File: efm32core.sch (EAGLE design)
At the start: 14 parts

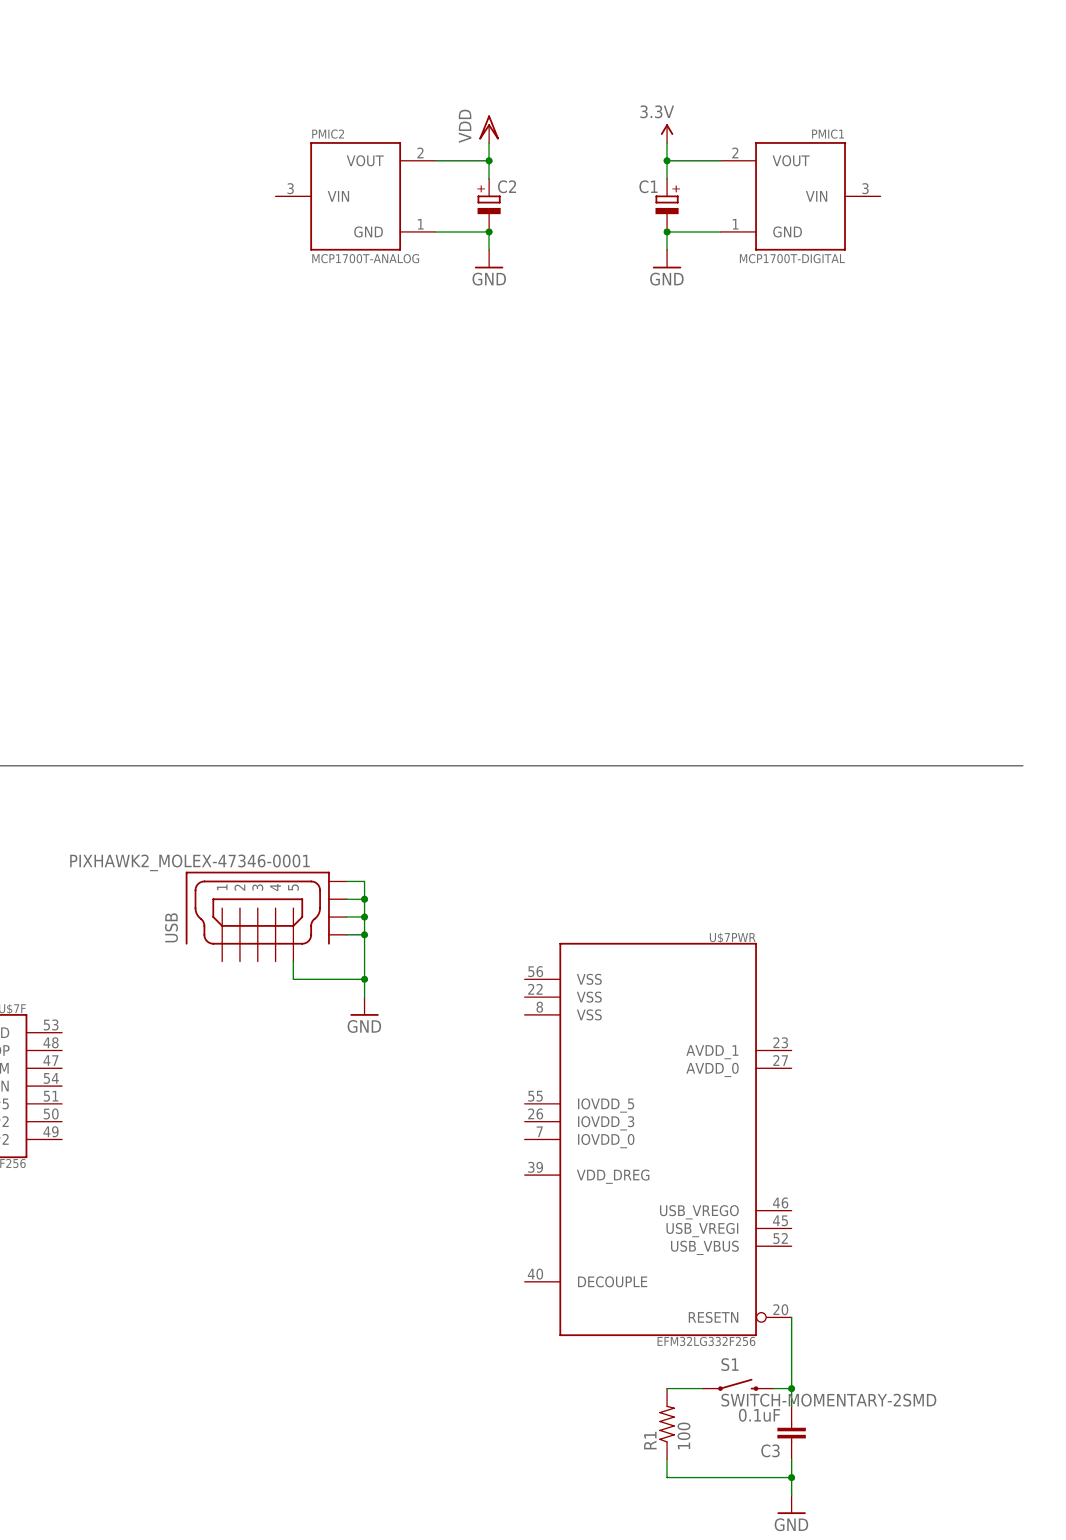
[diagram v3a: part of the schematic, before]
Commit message: optimize board shape
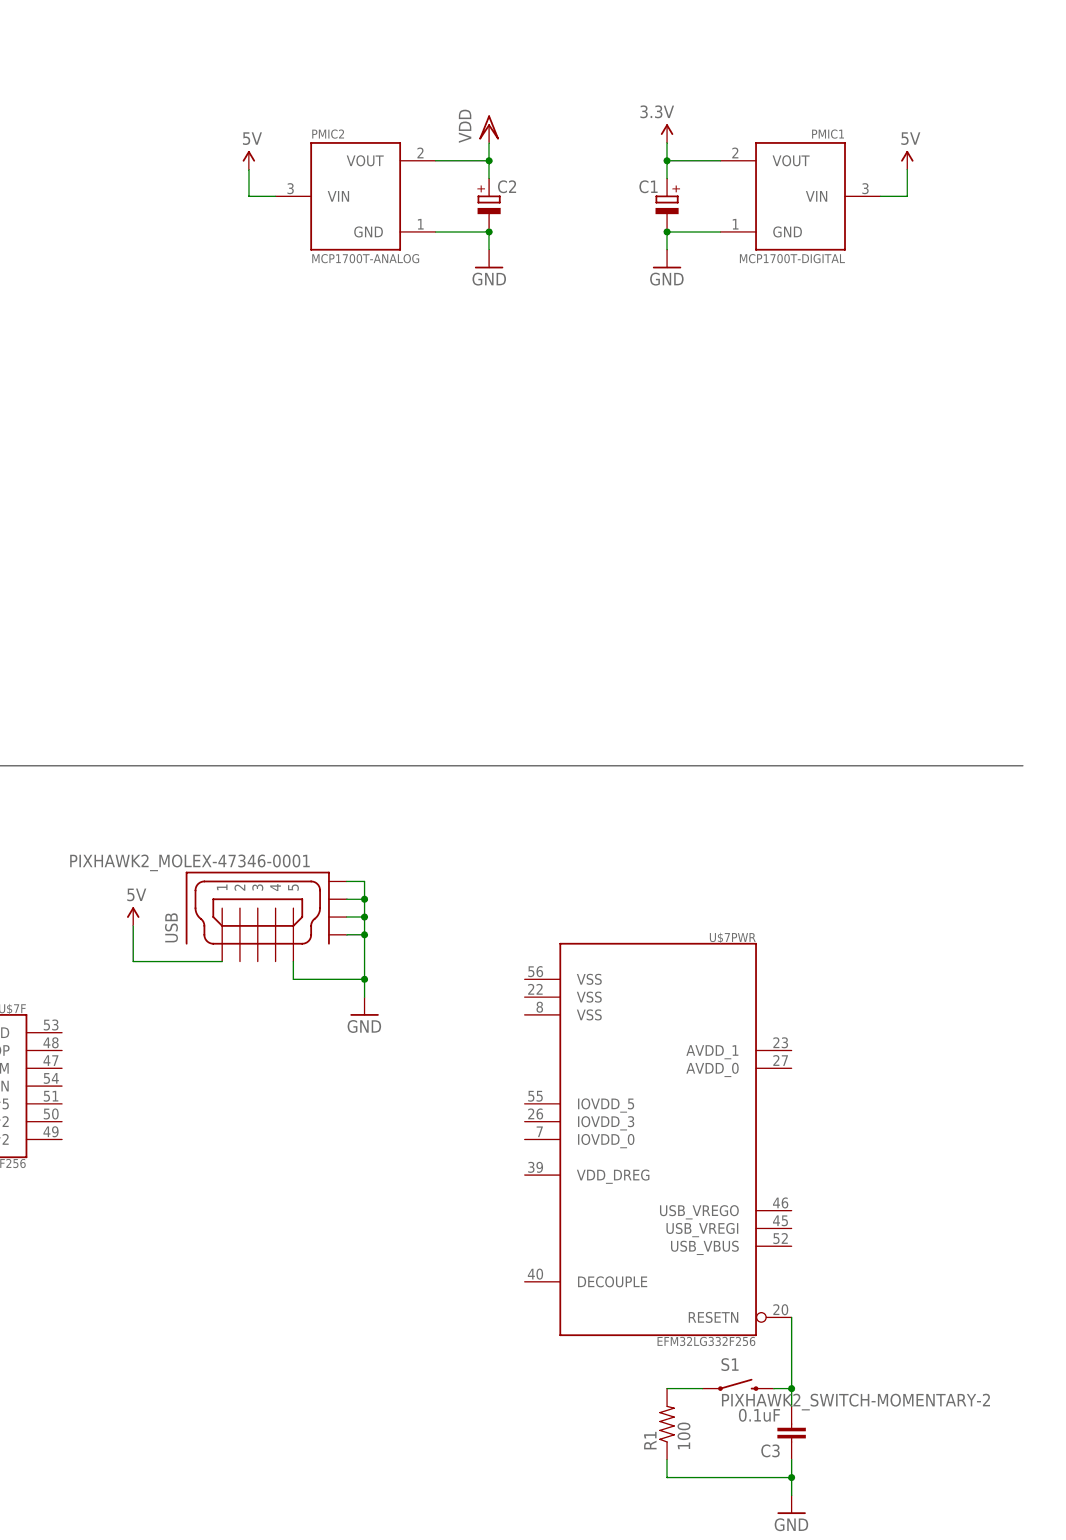
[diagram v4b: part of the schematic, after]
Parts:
- S1: value SWITCH-MOMENTARY-2SMD -> PIXHAWK2_SWITCH-MOMENTARY-2; device SparkFun-Electromechanical:SWITCH-MOMENTARY-2SMD -> PX4FMUv1.7.1:PIXHAWK2_SWITCH-MOMENTARY-2
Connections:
- new net 5V: PMIC1.VIN, PMIC2.VIN, USB.1
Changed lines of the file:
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@@
 <grid distance="0.05" unitdist="inch" unit="inch" style="lines" multiple="1" display="yes" altdistance="0.01" altunitdist="inch" altunit="inch"/>
 <layers>
-<layer number="1" name="Top" color="4" fill="1" visible="no" active="no"/>
-<layer number="16" name="Bottom" color="1" fill="1" visible="no" active="no"/>
-<layer number="17" name="Pads" color="2" fill="1" visible="no" active="no"/>
-<layer number="18" name="Vias" color="2" fill="1" visible="no" active="no"/>
-<layer number="19" name="Unrouted" color="6" fill="1" visible="no" active="no"/>
-<layer number="20" name="Dimension" color="15" fill="1" visible="no" active="no"/>
-<layer number="21" name="tPlace" color="7" fill="1" visible="no" active="no"/>
-<layer number="22" name="bPlace" color="7" fill="1" visible="no" active="no"/>
-<layer number="23" name="tOrigins" color="15" fill="1" visible="no" active="no"/>
-<layer number="24" name="bOrigins" color="15" fill="1" visible="no" active="no"/>
-<layer number="25" name="tNames" color="7" fill="1" visible="no" active="no"/>
-<layer number="26" name="bNames" color="7" fill="1" visible="no" active="no"/>
-<layer number="27" name="tValues" color="7" fill="1" visible="no" active="no"/>
-<layer number="28" name="bValues" color="7" fill="1" visible="no" active="no"/>
+<layer number="1" name="Top" color="4" fill="1" visible="yes" active="no"/>
+<layer number="16" name="Bottom" color="1" fill="1" visible="yes" active="no"/>
+<layer number="17" name="Pads" color="2" fill="1" visible="yes" active="no"/>
+<layer number="18" name="Vias" color="2" fill="1" visible="yes" active="no"/>
+<layer number="19" name="Unrouted" color="6" fill="1" visible="yes" active="no"/>
+<layer number="20" name="Dimension" color="15" fill="1" visible="yes" active="no"/>
+<layer number="21" name="tPlace" color="7" fill="1" visible="yes" active="no"/>
+<layer number="22" name="bPlace" color="7" fill="1" visible="yes" active="no"/>
+<layer number="23" name="tOrigins" color="15" fill="1" visible="yes" active="no"/>
+<layer number="24" name="bOrigins" color="15" fill="1" visible="yes" active="no"/>
+<layer number="25" name="tNames" color="7" fill="1" visible="yes" active="no"/>
+<layer number="26" name="bNames" color="7" fill="1" visible="yes" active="no"/>
+<layer number="27" name="tValues" color="7" fill="1" visible="yes" active="no"/>
+<layer number="28" name="bValues" color="7" fill="1" visible="yes" active="no"/>
 <layer number="29" name="tStop" color="7" fill="3" visible="no" active="no"/>
 <layer number="30" name="bStop" color="7" fill="6" visible="no" active="no"/>
@@
 <layer number="35" name="tGlue" color="7" fill="4" visible="no" active="no"/>
 <layer number="36" name="bGlue" color="7" fill="5" visible="no" active="no"/>
-<layer number="37" name="tTest" color="7" fill="1" visible="no" active="no"/>
-<layer number="38" name="bTest" color="7" fill="1" visible="no" active="no"/>
+<layer number="37" name="tTest" color="7" fill="1" visible="yes" active="no"/>
+<layer number="38" name="bTest" color="7" fill="1" visible="yes" active="no"/>
 <layer number="39" name="tKeepout" color="4" fill="11" visible="no" active="no"/>
 <layer number="40" name="bKeepout" color="1" fill="11" visible="no" active="no"/>
@@
 <layer number="44" name="Drills" color="7" fill="1" visible="no" active="no"/>
 <layer number="45" name="Holes" color="7" fill="1" visible="no" active="no"/>
-<layer number="46" name="Milling" color="3" fill="1" visible="no" active="no"/>
-<layer number="47" name="Measures" color="7" fill="1" visible="no" active="no"/>
-<layer number="48" name="Document" color="7" fill="1" visible="no" active="no"/>
-<layer number="49" name="Reference" color="7" fill="1" visible="no" active="no"/>
-<layer number="50" name="dxf" color="7" fill="1" visible="no" active="no"/>
-<layer number="51" name="tDocu" color="7" fill="1" visible="no" active="no"/>
-<layer number="52" name="bDocu" color="7" fill="1" visible="no" active="no"/>
-<layer number="53" name="tGND_GNDA" color="7" fill="9" visible="no" active="no"/>
-<layer number="54" name="bGND_GNDA" color="1" fill="9" visible="no" active="no"/>
-<layer number="56" name="wert" color="7" fill="1" visible="no" active="no"/>
-<layer number="57" name="tCAD" color="7" fill="1" visible="no" active="no"/>
-<layer number="58" name="bCAD" color="7" fill="1" visible="no" active="no"/>
+<layer number="46" name="Milling" color="3" fill="1" visible="yes" active="no"/>
+<layer number="47" name="Measures" color="7" fill="1" visible="yes" active="no"/>
+<layer number="48" name="Document" color="7" fill="1" visible="yes" active="no"/>
+<layer number="49" name="Reference" color="7" fill="1" visible="yes" active="no"/>
+<layer number="50" name="dxf" color="7" fill="1" visible="yes" active="no"/>
+<layer number="51" name="tDocu" color="14" fill="1" visible="yes" active="no"/>
+<layer number="52" name="bDocu" color="6" fill="1" visible="yes" active="no"/>
+<layer number="53" name="tGND_GNDA" color="7" fill="9" visible="yes" active="no"/>
+<layer number="54" name="bGND_GNDA" color="1" fill="9" visible="yes" active="no"/>
+<layer number="56" name="wert" color="7" fill="1" visible="yes" active="no"/>
+<layer number="57" name="tCAD" color="7" fill="1" visible="yes" active="no"/>
+<layer number="58" name="bCAD" color="7" fill="1" visible="yes" active="no"/>
 <layer number="91" name="Nets" color="2" fill="1" visible="yes" active="yes"/>
 <layer number="92" name="Busses" color="1" fill="1" visible="yes" active="yes"/>
@@
 <part name="C1" library="maple-r5" deviceset="CPOL-EU" device="UD-4X5,8"/>
 <part name="C2" library="maple-r5" deviceset="CPOL-EU" device="UD-4X5,8"/>
-<part name="SUPPLY1" library="SparkFun-Aesthetics" deviceset="3.3V" device=""/>
+<part name="3.3V" library="SparkFun-Aesthetics" deviceset="3.3V" device=""/>
 <part name="GND2" library="SparkFun-Aesthetics" deviceset="GND" device=""/>
 <part name="VDDA" library="maple-r5" deviceset="VDD" device=""/>
 <part name="GND1" library="SparkFun-Aesthetics" deviceset="GND" device=""/>
-<part name="S1" library="SparkFun-Electromechanical" deviceset="SWITCH-MOMENTARY-2" device="SMD"/>
 <part name="R1" library="SparkFun-Resistors" deviceset="100OHM1/10W1%(0603)" device="" value="100"/>
 <part name="C3" library="SparkFun-Capacitors" deviceset="0.1UF-25V-5%(0603)" device="" value="0.1uF"/>
@@
 <part name="USB" library="PX4FMUv1.7.1" deviceset="PIXHAWK2_MOLEX-47346-0001" device=""/>
 <part name="GND4" library="SparkFun-Aesthetics" deviceset="GND" device=""/>
+<part name="S1" library="PX4FMUv1.7.1" deviceset="PIXHAWK2_SWITCH-MOMENTARY-2" device=""/>
+<part name="5V" library="SparkFun-Aesthetics" deviceset="5V" device=""/>
+<part name="5V1" library="SparkFun-Aesthetics" deviceset="5V" device=""/>
+<part name="5V2" library="SparkFun-Aesthetics" deviceset="5V" device=""/>
 </parts>
 <sheets>
@@
 <instance part="C1" gate="G$1" x="330.2" y="215.9" rot="MR0"/>
 <instance part="C2" gate="G$1" x="304.8" y="215.9"/>
-<instance part="SUPPLY1" gate="G$1" x="330.2" y="223.52" rot="MR0"/>
+<instance part="3.3V" gate="G$1" x="330.2" y="223.52" rot="MR0"/>
 <instance part="GND2" gate="1" x="330.2" y="205.74"/>
 <instance part="VDDA" gate="G$1" x="304.8" y="226.06"/>
 <instance part="GND1" gate="1" x="304.8" y="205.74" rot="MR0"/>
-<instance part="S1" gate="G$1" x="340.36" y="45.72"/>
 <instance part="R1" gate="G$1" x="330.2" y="40.64" rot="R90"/>
 <instance part="C3" gate="G$1" x="347.98" y="40.64" rot="R180"/>
@@
 <instance part="USB" gate="G$1" x="271.78" y="111.76" rot="R90"/>
 <instance part="GND4" gate="1" x="287.02" y="99.06"/>
+<instance part="S1" gate="G$1" x="340.36" y="45.72"/>
+<instance part="5V" gate="G$1" x="254" y="111.76"/>
+<instance part="5V1" gate="G$1" x="270.51" y="219.71"/>
+<instance part="5V2" gate="G$1" x="364.49" y="219.71"/>
 </instances>
 <busses>
@@
 <pinref part="C1" gate="G$1" pin="+"/>
 <wire x1="330.2" y1="220.98" x2="330.2" y2="218.44" width="0.1524" layer="91"/>
-<pinref part="SUPPLY1" gate="G$1" pin="3.3V"/>
+<pinref part="3.3V" gate="G$1" pin="3.3V"/>
 <wire x1="330.2" y1="223.52" x2="330.2" y2="220.98" width="0.1524" layer="91"/>
 <junction x="330.2" y="220.98"/>
@@
 <pinref part="U$7" gate="PWR" pin="RESETN"/>
 <wire x1="347.98" y1="55.88" x2="347.98" y2="45.72" width="0.1524" layer="91"/>
-<pinref part="S1" gate="G$1" pin="2"/>
 <wire x1="347.98" y1="45.72" x2="345.44" y2="45.72" width="0.1524" layer="91"/>
 <pinref part="C3" gate="G$1" pin="2"/>
 <wire x1="347.98" y1="43.18" x2="347.98" y2="45.72" width="0.1524" layer="91"/>
 <junction x="347.98" y="45.72"/>
+<pinref part="S1" gate="G$1" pin="2"/>
 </segment>
 </net>
 <net name="N$6" class="0">
 <segment>
-<pinref part="S1" gate="G$1" pin="1"/>
 <pinref part="R1" gate="G$1" pin="2"/>
 <wire x1="335.28" y1="45.72" x2="330.2" y2="45.72" width="0.1524" layer="91"/>
-</segment>
-</net>
+<pinref part="S1" gate="G$1" pin="1"/>
+</segment>
+</net>
+<net name="5V" class="0">
+<segment>
+<pinref part="USB" gate="G$1" pin="1"/>
+<wire x1="266.7" y1="106.68" x2="254" y2="106.68" width="0.1524" layer="91"/>
+<wire x1="254" y1="106.68" x2="254" y2="111.76" width="0.1524" layer="91"/>
+<pinref part="5V" gate="G$1" pin="5V"/>
+</segment>
+<segment>
+<pinref part="5V1" gate="G$1" pin="5V"/>
+<wire x1="270.51" y1="219.71" x2="270.51" y2="215.9" width="0.1524" layer="91"/>
+<pinref part="PMIC2" gate="G$1" pin="VIN"/>
+<wire x1="270.51" y1="215.9" x2="274.32" y2="215.9" width="0.1524" layer="91"/>
+</segment>
+<segment>
+<pinref part="PMIC1" gate="G$1" pin="VIN"/>
+<wire x1="360.68" y1="215.9" x2="364.49" y2="215.9" width="0.1524" layer="91"/>
+<pinref part="5V2" gate="G$1" pin="5V"/>
+<wire x1="364.49" y1="215.9" x2="364.49" y2="219.71" width="0.1524" layer="91"/>
+</segment>
+</net>
